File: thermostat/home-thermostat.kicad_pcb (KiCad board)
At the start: 2 copper layers, 146 x 79.5 mm, 100 parts, among them J1 Thermosthat, J2 Conn_01x24, J3 Conn_01x06, J4 AVR-ISP-6, Q1 BC817, Q2 BC817, Q3 BSS806NL6327, Q4 BC817, Q5 BSS806NL6327, Q6 BC817, Q7 BSS806NL6327, SW1 UP, SW2 DOWN, SW3 LEFT, SW4 RIGHT, SW5 OK, SW6 CANCEL, U1 ESP-12F, U2 MCP7940N-xMS, U3 LM2574M-5, U4 LD1117S33TR_SOT223, U5 AT24C512, U6 ATmega328P-AU, U7 LM358, U8 MCP9844, Y1 GEY KX-327NHT 12, Y2 20MHz ABM3B

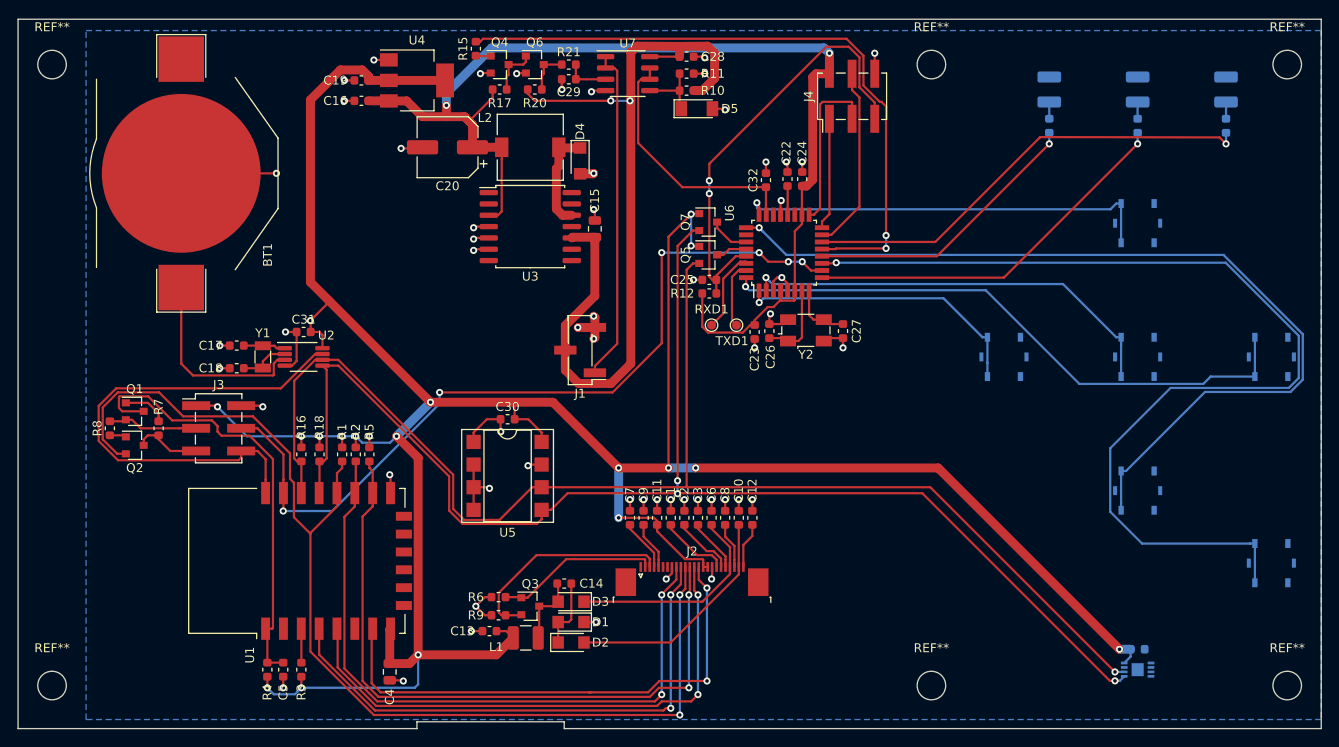
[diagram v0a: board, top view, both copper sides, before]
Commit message: Updated symbols after library update, some footprints still need to be assigned. Deleted PCB except for Display and buttons. Button arrangement wrong. Move buttons to other side of Display. Maybe put buttons on separate PCB and create one PCB for MCU and logic, since that needs to be a four layer one. That is expensive and should be kept as small as possible.
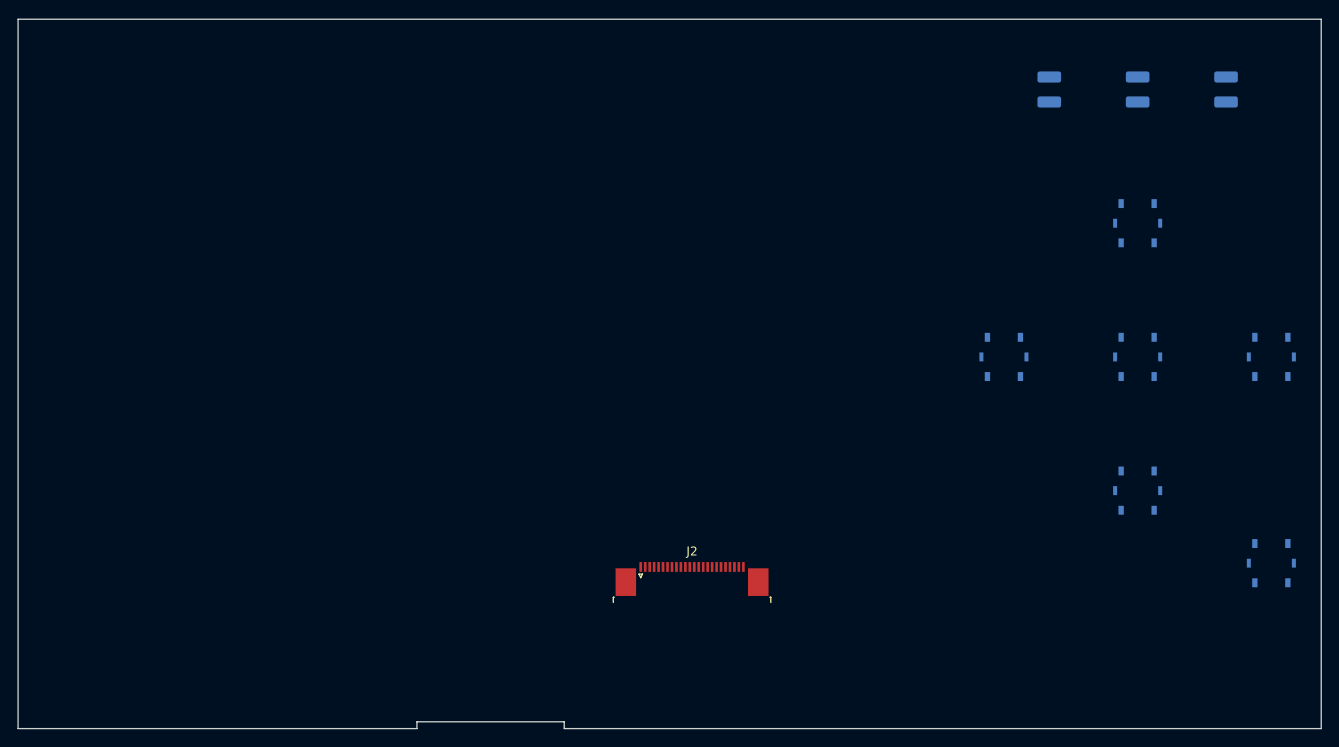
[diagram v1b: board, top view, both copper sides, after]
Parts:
- removed BT1: Battery_Cell, Battery:BatteryHolder_Keystone_3002_1x2032
- removed C1, C10, C12, C2, C29, C3, C6, C7, C8, C9: 1u, Capacitor_SMD:C_0603_1608Metric
- removed C11, C14, C16, C22, C23, C24, C28, C5: 100n, Capacitor_SMD:C_0603_1608Metric
- removed C13: 4u7, Capacitor_SMD:C_0603_1608Metric
- removed C15: 22u, Capacitor_SMD:C_0805_2012Metric
- removed C17, C18: 10p, Capacitor_SMD:C_0603_1608Metric
- removed C19: 2u2, Capacitor_SMD:C_0603_1608Metric
- removed C20: 220u, Capacitor_SMD:CP_Elec_6.3x5.4
- removed C21, C30, C31, C32: 10n, Capacitor_SMD:C_0603_1608Metric
- removed C25: 47n, Capacitor_SMD:C_0603_1608Metric
- removed C26, C27: 15p, Capacitor_SMD:C_0603_1608Metric
- removed C4: 100u, Capacitor_SMD:C_0805_2012Metric
- removed D1, D2, D3, D4: SL03, Diode_SMD:D_SMF
- removed D5: ZMM3V3, Diode_SMD:D_MiniMELF
- removed J1: Thermosthat, Connector_PinHeader_2.54mm:PinHeader_1x03_P2.54mm_Vertical_SMD_Pin1Left
- removed J3: Conn_01x06, Connector_PinHeader_2.54mm:PinHeader_2x03_P2.54mm_Vertical_SMD
- removed J4: AVR-ISP-6, Connector_PinHeader_2.54mm:PinHeader_2x03_P2.54mm_Vertical_SMD
- removed L1: 68u, Inductor_SMD:L_1210_3225Metric
- removed L2: 330u, Inductor_SMD:L_7.3x7.3_H3.5
- removed Q1, Q2, Q4, Q6: BC817, Package_TO_SOT_SMD:SOT-23
- removed Q3, Q5, Q7: BSS806NL6327, Package_TO_SOT_SMD:SOT-23
- removed R1, R10, R12, R2, R20, R3, R4, R5, R6, R7, R8: 10K, Resistor_SMD:R_0603_1608Metric
- removed R11, R21: 1K, Resistor_SMD:R_0603_1608Metric
- removed R13, R14, R19: 1K8, Resistor_SMD:R_0603_1608Metric
- removed R15, R16, R17, R18: 4K7, Resistor_SMD:R_0603_1608Metric
- removed R9: 0.47R, Resistor_SMD:R_0603_1608Metric
- removed REF** (x6): MountingHole_3.2mm_M3, MountingHole:MountingHole_3.2mm_M3
- removed RXD1: RXD, TestPoint:TestPoint_Pad_D1.0mm
- removed TXD1: TXD, TestPoint:TestPoint_Pad_D1.0mm
- removed U1: ESP-12F, RF_Module:ESP-12E
- removed U2: MCP7940N-xMS, Package_SO:MSOP-8_3x3mm_P0.65mm
- removed U3: LM2574M-5, Package_SO:SOIC-14W_7.5x9mm_P1.27mm
- removed U4: LD1117S33TR_SOT223, Package_TO_SOT_SMD:SOT-223-3_TabPin2
- removed U5: AT24C512, Package_DIP:DIP-8_W7.62mm_SMDSocket_SmallPads
- removed U6: ATmega328P-AU, Package_QFP:TQFP-32_7x7mm_P0.8mm
- removed U7: LM358, Package_SO:SOIC-8_3.9x4.9mm_P1.27mm
- removed U8: MCP9844, Package_DFN_QFN:DFN-8-1EP_3x2mm_P0.5mm_EP1.36x1.46mm
- removed Y1: GEY KX-327NHT 12, Crystal:Crystal_SMD_3215-2Pin_3.2x1.5mm
- removed Y2: 20MHz ABM3B, Crystal:Crystal_SMD_Abracon_ABM3B-4Pin_5.0x3.2mm
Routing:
- net +3V3: track 321.8 -> 0.00 mm, vias 18 -> 0
- net /SDA: track 156.5 -> 0.00 mm, vias 3 -> 0
- net /SCL: track 153.1 -> 0.00 mm, vias 1 -> 0
- net +5V: track 127.6 -> 0.00 mm, vias 2 -> 0
- net /GPIO0: track 125.3 -> 0.00 mm, vias 2 -> 0
- net /regulator_out/CANCEL: track 115.2 -> 0.00 mm, vias 1 -> 0
- net GND: track 112.8 -> 0.00 mm, vias 56 -> 0
- net /regulator_out/DOWN: track 101.4 -> 0.00 mm, vias 1 -> 0
- net +36V: track 95.3 -> 0.00 mm, vias 2 -> 0
- net /AVR_INT: track 92.2 -> 0.00 mm, vias 6 -> 0
- net /GPIO15: track 76.6 -> 0.00 mm, vias 2 -> 0
- net /GPIO2: track 76.1 -> 0.00 mm, vias 2 -> 0
- net /regulator_out/pwm_sig: track 74.3 -> 0.00 mm, vias 2 -> 0
- net /regulator_out/LEFT: track 67.4 -> 0.00 mm, vias 1 -> 0
- net /SCK: track 61.5 -> 0.00 mm, vias 2 -> 0
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- removed copper zone on B.Cu, net GND

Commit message: Finalized Thermostat circuit based on the MKW41Z.
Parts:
- added BT1: Battery_Cell, Battery:BatteryHolder_Keystone_3002_1x2032, F.Cu at (49.4, 33.8)
- added C1: 0,1u, Capacitor_SMD:C_0402_1005Metric, F.Cu at (34.5, 77.1)
- added C10: 0,1u, Capacitor_SMD:C_0402_1005Metric, F.Cu at (52.7, 76.9)
- added C11: 0,1u, Capacitor_SMD:C_0402_1005Metric, F.Cu at (55.6, 76.9)
- added C12: 0, Capacitor_SMD:C_0603_1608Metric, F.Cu at (45.4, 46.7)
- added C13: 10p, Capacitor_SMD:C_0402_1005Metric, F.Cu at (76.7, 62.3)
- added C14: 1n, Capacitor_SMD:C_0603_1608Metric, F.Cu at (58.9, 69.2)
- added C15: 1u, Capacitor_SMD:C_0603_1608Metric, F.Cu at (138.1, 35.0)
- added C16: 1u, Capacitor_SMD:C_0603_1608Metric, F.Cu at (142.1, 34.2)
- added C17: 1u, Capacitor_SMD:C_0603_1608Metric, F.Cu at (150.1, 36.9)
- added C18: 1u, Capacitor_SMD:C_0603_1608Metric, F.Cu at (134.1, 35.0)
- added C19: 1u, Capacitor_SMD:C_0603_1608Metric, F.Cu at (150.1, 34.4)
- added C2: 10u, Capacitor_SMD:C_0603_1608Metric, F.Cu at (58.9, 71.8)
- added C20: 1u, Capacitor_SMD:C_0603_1608Metric, F.Cu at (140.0, 31.7)
- added C21: 1u, Capacitor_SMD:C_0603_1608Metric, F.Cu at (146.1, 36.9)
- added C22: 1u, Capacitor_SMD:C_0603_1608Metric, F.Cu at (150.1, 31.9)
- added C23: 100n, Capacitor_SMD:C_0603_1608Metric, F.Cu at (146.1, 34.4)
- added C24: 1u, Capacitor_SMD:C_0603_1608Metric, F.Cu at (152.4, 27.3)
- added C25: 10u, Capacitor_SMD:C_0603_1608Metric, F.Cu at (146.1, 31.9)
- added C26: 4u7, Capacitor_SMD:C_0603_1608Metric, F.Cu at (134.1, 37.5)
- added C27: 10n, Capacitor_SMD:C_0603_1608Metric, F.Cu at (75.2, 35.8)
- added C28: 0, Capacitor_SMD:C_0603_1608Metric, F.Cu at (61.4, 46.7)
- added C29: 0,1u, Capacitor_SMD:C_0603_1608Metric, F.Cu at (46.3, 77.1)
- added C3: 1u, Capacitor_SMD:C_0402_1005Metric, F.Cu at (58.5, 76.5)
- added C30: 10n, Capacitor_SMD:C_0603_1608Metric, F.Cu at (49.4, 46.7)
- added C31: 1u, Capacitor_SMD:C_0603_1608Metric, F.Cu at (53.4, 46.7)
- added C32: 22u, Capacitor_SMD:C_0805_2012Metric, F.Cu at (117.1, 56.9)
- added C33: 100n, Capacitor_SMD:C_0603_1608Metric, F.Cu at (116.2, 62.2)
- added C34: 2u2, Capacitor_SMD:C_0603_1608Metric, F.Cu at (116.9, 59.6)
- added C35: 220u, Capacitor_SMD:CP_Elec_6.3x5.4, F.Cu at (88.0, 66.7)
- added C36: 10n, Capacitor_SMD:C_0603_1608Metric, F.Cu at (107.8, 71.2)
- added C37: 1u, Capacitor_SMD:C_0603_1608Metric, F.Cu at (103.3, 73.2)
- added C38: 100n, Capacitor_SMD:C_0603_1608Metric, F.Cu at (107.8, 68.6)
- added C39: 1n, Capacitor_SMD:C_0603_1608Metric, F.Cu at (88.9, 43.3)
- added C4: 0,1u, Capacitor_SMD:C_0402_1005Metric, F.Cu at (65.4, 74.6)
- added C40: 1n, Capacitor_SMD:C_0603_1608Metric, F.Cu at (110.1, 40.0)
- added C41: 1n, Capacitor_SMD:C_0603_1608Metric, F.Cu at (110.1, 42.5)
- added C42: 1n, Capacitor_SMD:C_0603_1608Metric, F.Cu at (117.7, 33.9)
- added C43: 1n, Capacitor_SMD:C_0603_1608Metric, F.Cu at (114.1, 38.5)
- added C44: 1n, Capacitor_SMD:C_0603_1608Metric, F.Cu at (114.1, 41.0)
- added C45: 100n, Capacitor_SMD:C_0603_1608Metric, F.Cu at (118.2, 36.4)
- added C46: 1u, Capacitor_SMD:C_0603_1608Metric, F.Cu at (75.6, 53.3)
- added C47: 1u, Capacitor_SMD:C_0603_1608Metric, F.Cu at (75.2, 57.0)
- added C48: 0,1u, Capacitor_SMD:C_0603_1608Metric, F.Cu at (62.9, 68.7)
- added C49: 1u, Capacitor_SMD:C_0603_1608Metric, F.Cu at (111.8, 66.7)
- added C5: 10p, Capacitor_SMD:C_0402_1005Metric, F.Cu at (69.4, 68.2)
- added C6: 12p, Capacitor_SMD:C_0402_1005Metric, F.Cu at (69.2, 66.2)
- added C7: 12p, Capacitor_SMD:C_0402_1005Metric, F.Cu at (69.4, 70.2)
- added C8: 1u, Capacitor_SMD:C_0603_1608Metric, F.Cu at (70.2, 60.3)
- added C9: 0,7p, Capacitor_SMD:C_0402_1005Metric, F.Cu at (49.8, 76.9)
- added D1: LED, LED_SMD:LED_1210_3225Metric, F.Cu at (41.5, 74.4)
- added D2: SL03, Diode_SMD:D_SMF, F.Cu at (135.1, 32.1)
- added D3: SL03, Diode_SMD:D_SMF, F.Cu at (148.9, 24.4)
- added D4: SL03, Diode_SMD:D_SMF, F.Cu at (129.4, 32.1)
- added D5: SL03, Diode_SMD:D_SMF, F.Cu at (117.8, 53.8)
- added D9: RED, LED_SMD:LED_1210_3225Metric, F.Cu at (100.9, 39.8)
- added J1: Amphenol_132289 SMA, Connector_Coaxial:SMA_Amphenol_132289_EdgeMount, F.Cu at (37.3, 58.2)
- added J3: Thermosthat, Connector_PinHeader_2.54mm:PinHeader_1x03_P2.54mm_Vertical_SMD_Pin1Left, F.Cu at (97.3, 67.5)
- added JP1: SolderJumper_3_Open, Jumper:SolderJumper-3_P1.3mm_Open_Pad1.0x1.5mm, F.Cu at (35.9, 74.0)
- added JP2: SolderJumper_2_Open, Jumper:SolderJumper-2_P1.3mm_Open_Pad1.0x1.5mm, F.Cu at (46.5, 74.0)
- added L1: 0,1u, Inductor_SMD:L_0402_1005Metric, F.Cu at (61.4, 77.1)
- added L2: 5,6n, Inductor_SMD:L_0402_1005Metric, F.Cu at (72.2, 66.2)
- added L3: 68u, Inductor_SMD:L_1210_3225Metric, F.Cu at (129.3, 35.9)
- added L4: 330u, Inductor_SMD:L_7.3x7.3_H3.5, F.Cu at (110.2, 56.5)
- added L5: 0,1u, Inductor_SMD:L_0402_1005Metric, F.Cu at (72.3, 68.2)
- added Q1: BSS806NL6327, Package_TO_SOT_SMD:SOT-23, F.Cu at (148.2, 28.3)
- added Q2: BC817, Package_TO_SOT_SMD:SOT-23, F.Cu at (112.0, 63.2)
- added Q3: BC817, Package_TO_SOT_SMD:SOT-23, F.Cu at (103.5, 69.7)
- added Q4: BC817, Package_TO_SOT_SMD:SOT-23, F.Cu at (105.9, 41.0)
- added Q5: BC817, Package_TO_SOT_SMD:SOT-23, F.Cu at (120.7, 25.0)
- added Q6: BC817, Package_TO_SOT_SMD:SOT-23, F.Cu at (113.5, 32.4)
- added R10: 4K7, Resistor_SMD:R_0603_1608Metric, F.Cu at (116.2, 64.7)
- added R11: 10K, Resistor_SMD:R_0603_1608Metric, F.Cu at (111.8, 69.3)
- added R12: 1K, Resistor_SMD:R_0603_1608Metric, F.Cu at (91.1, 72.0)
- added R13: 0, Resistor_SMD:R_0603_1608Metric, F.Cu at (93.0, 43.3)
- added R14: 0, Resistor_SMD:R_0603_1608Metric, F.Cu at (97.0, 43.3)
- added R15: 0, Resistor_SMD:R_0603_1608Metric, F.Cu at (101.0, 43.2)
- added R16: 100k, Resistor_SMD:R_0603_1608Metric, F.Cu at (120.5, 28.5)
- added R17: 100k, Resistor_SMD:R_0603_1608Metric, F.Cu at (113.2, 36.0)
- added R18: 100k, Resistor_SMD:R_0603_1608Metric, F.Cu at (117.7, 31.4)
- added R19: 100k, Resistor_SMD:R_0603_1608Metric, F.Cu at (84.9, 43.3)
- added R2: 0, Resistor_SMD:R_0603_1608Metric, F.Cu at (58.9, 74.3)
- added R3: 10K, Resistor_SMD:R_0603_1608Metric, F.Cu at (142.1, 36.7)
- added R4: 0.47R, Resistor_SMD:R_0603_1608Metric, F.Cu at (138.1, 37.5)
- added R5: 2k2, Resistor_SMD:R_0603_1608Metric, F.Cu at (67.8, 40.4)
- added R6: 2k2, Resistor_SMD:R_0603_1608Metric, F.Cu at (57.4, 46.7)
- added R7: 10K, Resistor_SMD:R_0603_1608Metric, F.Cu at (120.2, 64.7)
- added R8: 1K, Resistor_SMD:R_0603_1608Metric, F.Cu at (115.8, 67.2)
- added R9: 4K7, Resistor_SMD:R_0603_1608Metric, F.Cu at (120.2, 62.2)
- added SW7: CANCEL, Button_Switch_SMD:SW_SPST_Panasonic_EVQPL_3PL_5PL_PT_A08, F.Cu at (114.7, 26.4)
- added TP1: TestPoint, TestPoint:TestPoint_Pad_D1.0mm, F.Cu at (50.5, 65.8)
- added TP10: ~RST, TestPoint:TestPoint_Pad_D1.0mm, F.Cu at (62.4, 74.6)
- added TP11: SWD_DIO, TestPoint:TestPoint_Pad_D1.0mm, F.Cu at (66.4, 69.0)
- added TP12: SWD_CLK, TestPoint:TestPoint_Pad_D1.0mm, F.Cu at (76.8, 59.8)
- added TP13: UART_TX, TestPoint:TestPoint_Pad_D1.0mm, F.Cu at (73.7, 60.6)
- added TP14: SUPPLY_V, TestPoint:TestPoint_Pad_D1.0mm, F.Cu at (62.4, 71.5)
- added TP2: TestPoint, MountingHole:MountingHole_3.2mm_M3, F.Cu at (64.2, 56.1)
- added TP3: TestPoint, MountingHole:MountingHole_3.2mm_M3, F.Cu at (37.0, 68.3)
- added TP4: TestPoint, MountingHole:MountingHole_3.2mm_M3, F.Cu at (45.0, 68.3)
- added TP5: TestPoint, MountingHole:MountingHole_3.2mm_M3, F.Cu at (56.3, 56.1)
- added TP6: TestPoint, MountingHole:MountingHole_3.2mm_M3, F.Cu at (56.3, 64.0)
- added TP7: TestPoint, MountingHole:MountingHole_3.2mm_M3, F.Cu at (52.9, 72.0)
- added TP8: 3V3, TestPoint:TestPoint_Pad_D1.0mm, F.Cu at (65.5, 72.1)
- added TP9: GND, TestPoint:TestPoint_Pad_D1.0mm, F.Cu at (73.2, 63.7)
- added U1: MKW41Z512VHT, Package_DFN_QFN:NXP_LQFN-48-1EP_7x7mm_P0.5mm_EP3.5x3.5mm_16xMask0.45x0.45_ThermalVias, F.Cu at (71.1, 106.0)
- added U2: MCP7940N-xMS, Package_SO:MSOP-8_3x3mm_P0.65mm, F.Cu at (69.5, 36.8)
- added U3: MCP9844, Package_DFN_QFN:DFN-8-1EP_3x2mm_P0.5mm_EP1.36x1.46mm, F.Cu at (35.7, 47.2)
- added U4: AT24C512, Package_DIP:DIP-8_W7.62mm_SMDSocket_SmallPads, F.Cu at (71.7, 28.6)
- added U5: LM2574M-5, Package_SO:SOIC-14W_7.5x9mm_P1.27mm, F.Cu at (89.2, 57.4)
- added U6: LD1117S33TR_SOT223, Package_TO_SOT_SMD:SOT-223-3_TabPin2, F.Cu at (100.5, 56.2)
- added U7: LM358, Package_SO:SOIC-8_3.9x4.9mm_P1.27mm, F.Cu at (105.5, 64.2)
- added U8: PCF8574, Package_SO:SOIC-16W_7.5x10.3mm_P1.27mm, F.Cu at (89.4, 28.6)
- added U9: SN74LVC2T45DCUR, Package_SO:VSSOP-8_2.4x2.1mm_P0.5mm, F.Cu at (70.9, 53.9)
- added Y1: 32MHz 10PPM SMT 2.0x1.6mm 10PF, Crystal:Crystal_SMD_2016-4Pin_2.0x1.6mm, F.Cu at (69.7, 63.4)
- added Y2: 32.768KHz 20PPM 3.2x1.5mm 7PF, Crystal:Crystal_SMD_3215-2Pin_3.2x1.5mm, F.Cu at (70.7, 57.4)
- added Y3: 32.768KHz 20PPM 3.2x1.5mm 7PF, Crystal:Crystal_SMD_3215-2Pin_3.2x1.5mm, F.Cu at (40.9, 47.1)
- D6: value YELLOW -> ZMM3V3; footprint LED_SMD:LED_1210_3225Metric -> Diode_SMD:D_MiniMELF; moved to F.Cu
- D7: value RED -> YELLOW; moved to F.Cu
- D8: moved to F.Cu
- SW1: value UP -> SW_Push; moved to F.Cu
- SW2: value DOWN -> UP; moved to F.Cu
- SW3: value LEFT -> DOWN; moved to F.Cu
- SW4: value RIGHT -> LEFT; moved to F.Cu
- SW5: value OK -> RIGHT; moved to F.Cu
- SW6: value CANCEL -> OK; moved to F.Cu
- moved J2 242.0 mm to (-68.7, 26.9)
- moved Waveshare 4.2 Inch raw panel 241.7 mm to (-91.2, 4.70)
- moved SW6 156.9 mm to (101.8, 33.9)
- moved SW2 147.4 mm to (86.7, 38.3)
- moved SW3 146.4 mm to (99.6, 26.4)
- moved SW1 132.2 mm to (64.0, 63.8)
- moved SW5 132.2 mm to (107.2, 26.4)
- moved SW4 121.4 mm to (94.3, 38.3)
- moved D8 111.6 mm to (108.4, 32.3), turned to 0 degrees
- moved D6 103.2 mm to (85.9, 72.4), turned to 0 degrees
- moved D7 94.1 mm to (108.4, 36.6), turned to 0 degrees
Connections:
- net /HLT_CTL renamed /display/HLT_CTL
- net /TSCL renamed /display/TSCL
- net /TSDA renamed /display/TSDA
- D6 pad 1: GND -> Net-(D6-Pad1)
- D6 pad 2: Net-(D6-Pad2) -> GND
- D7 pad 1: GND -> Net-(D7-Pad1)
- D8 pad 1: GND -> Net-(D8-Pad1)
- J2 pad 10: /eink-RST -> /~DP_RST
- J2 pad 11: /GPIO0 -> GND
- J2 pad 12: /GPIO15 -> /SPI1_PCS0
- J2 pad 13: /SCK -> /SPI1_SCK
- J2 pad 14: /MOSI -> /SPI1_MOSI
- J2 pad 18: /VDD -> /display/VDD
- J2 pad 19: /VPP -> /display/VPP
- J2 pad 2: /GDR -> /display/GDR
- J2 pad 20: /VSH -> /display/VSH
- J2 pad 21: /PREVGH -> /display/PREVGH
- J2 pad 22: /VSL -> /display/VSL
- J2 pad 23: /PREVGL -> /display/PREVGL
- J2 pad 24: /VCOM -> /display/VCOM
- J2 pad 3: /RESE -> /display/RESE
- J2 pad 4: /VGL -> /display/VGL
- J2 pad 5: /VGH -> /display/VGH
- J2 pad 8: GND -> +3V3
- J2 pad 9: /GPIO2 -> /DP_BUSY
- SW1 pad 1: /regulator_out/UP -> GND
- SW1 pad 2: GND -> /RESET_b
- SW2 pad 1: /regulator_out/DOWN -> /GPIO/BTN_UP
- SW3 pad 1: /regulator_out/LEFT -> /GPIO/BTN_DOWN
- SW4 pad 1: /regulator_out/RIGHT -> /GPIO/BTN_LEFT
- SW5 pad 1: /regulator_out/OK -> /GPIO/BTN_RIGHT
- SW6 pad 1: /regulator_out/CANCEL -> /BTN_OK

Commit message: Started grouping footprints on PCB, configured minimal via and trace sizes for PCB_POOL.
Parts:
- added C50: 0,1u, Capacitor_SMD:C_0402_1005Metric, F.Cu at (231.8, 106.8)
- added C51: 10u, Capacitor_SMD:C_0603_1608Metric, F.Cu at (232.8, 109.1)
- added C52: 1u, Capacitor_SMD:C_0402_1005Metric, F.Cu at (225.2, 107.4)
- added C53: 1u, Capacitor_SMD:C_0402_1005Metric, F.Cu at (225.7, 96.0)
- added C54: 10u, Capacitor_SMD:C_0603_1608Metric, F.Cu at (225.2, 109.7)
- added C55: 10u, Capacitor_SMD:C_0603_1608Metric, F.Cu at (225.7, 93.7)
- added L6: 0,1u, Inductor_SMD:L_0402_1005Metric, F.Cu at (224.2, 107.4)
- added L7: 0,1u, Inductor_SMD:L_0402_1005Metric, F.Cu at (226.7, 96.0)
- added TP15: 5V, TestPoint:TestPoint_Pad_D1.0mm, F.Cu at (58.9, 78.2)
- C8: footprint Capacitor_SMD:C_0603_1608Metric -> Capacitor_SMD:C_0402_1005Metric
- moved U3 241.5 mm to (256.8, 144.4)
- moved C30 227.7 mm to (256.8, 140.7)
- moved J1 214.9 mm to (248.0, 100.2)
- moved C1 185.2 mm to (218.6, 97.7)
- moved C9 182.6 mm to (231.0, 99.7), turned to 90 degrees
- moved C10 176.1 mm to (226.2, 107.4), turned to 270 degrees
- moved L1 174.9 mm to (233.8, 106.8), turned to 270 degrees
- moved C3 174.8 mm to (232.0, 97.5), turned to 90 degrees
- moved C2 174.7 mm to (232.0, 95.2)
- moved BT1 172.8 mm to (127.1, 188.1)
- moved C13 170.4 mm to (242.8, 100.2), turned to 180 degrees
- moved C4 170.2 mm to (233.4, 101.5)
- moved C31 170.2 mm to (198.4, 135.8)
- moved C11 170.1 mm to (224.7, 96.0), turned to 90 degrees
- moved C8 169.1 mm to (232.8, 106.8), turned to 270 degrees
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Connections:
- net Net-(C1-Pad1) renamed /VREF
- net Net-(C3-Pad1) renamed /VDD_RF
- net Net-(C5-Pad1) renamed /XTAL_O
- net Net-(C8-Pad1) renamed /VDDA
- C10 pad 1: +3V3 -> /VDD_0
- C11 pad 1: +3V3 -> /VDD_1
- U1 pad 20: +3V3 -> /VDD_0
- U1 pad 44: +3V3 -> /VDD_1
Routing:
- net /VDDA: track 0.00 -> 5.29 mm
- net Net-(U1-Pad30): track 0.00 -> 5.25 mm
- net /XTAL_O: track 0.00 -> 4.49 mm, vias 0 -> 1
- net /VDD_0: track 0.00 -> 4.17 mm
- net Net-(U1-Pad31): track 0.00 -> 3.09 mm
- net /VDD_RF: track 0.00 -> 2.03 mm
- net /VREF: track 0.00 -> 0.92 mm, vias 0 -> 1
- net (no net): vias 0 -> 16
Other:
- copper layers 2 -> 4
- net class Default: clearance 0.2 -> 0.15; trace_width 0.25 -> 0.15; via_dia 0.8 -> 0.5; via_drill 0.4 -> 0.2
- rule trace_clearance: 0.2 -> 0.15
- rule trace_min: 0.2 -> 0.15
- rule via_min_drill: 0.3 -> 0.2
- rule via_min_size: 0.4 -> 0.5

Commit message: Started routing some subgroups, going to put GPIO on other board and not attach display directly, as that would make the PCB too large and expensive.
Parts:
- removed Waveshare 4.2 Inch raw panel: waveshare_4.2_raw_panel, myfootprints:waveshare_4.2_raw_panel_folded_connector
- moved C14 314.3 mm to (286.8, -86.1)
- moved C29 314.3 mm to (310.5, -36.7)
- moved C30 314.3 mm to (512.8, -41.7)
- moved C31 314.3 mm to (454.4, -46.6)
- moved C32 314.3 mm to (496.6, -137.0)
- moved C33 314.3 mm to (473.0, -143.1)
- moved C34 314.3 mm to (467.7, -143.8)
- moved C35 314.3 mm to (494.9, -152.1)
- moved C37 314.3 mm to (444.1, -123.4)
- moved C38 314.3 mm to (456.6, -126.0)
- moved C39 314.3 mm to (345.0, -139.1)
- moved C40 314.3 mm to (366.2, -142.4)
- moved C41 314.3 mm to (366.2, -139.9)
- moved C42 314.3 mm to (373.7, -148.4)
- moved C43 314.3 mm to (370.2, -143.9)
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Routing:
- net +3V3: track 0.00 -> 14.7 mm
- net Net-(C26-Pad1): track 0.00 -> 12.2 mm
- net Net-(C26-Pad2): track 0.00 -> 7.80 mm
- net /display/VDD: track 0.00 -> 7.06 mm
- net /display/GDR: track 0.00 -> 6.91 mm
- net /display/VCOM: track 0.00 -> 6.86 mm
- net /display/VPP: track 0.00 -> 6.64 mm
- net /display/RESE: track 0.00 -> 6.48 mm
- net /display/PREVGL: track 0.00 -> 6.28 mm
- net /display/VSH: track 0.00 -> 6.22 mm
- net /display/VGL: track 0.00 -> 6.06 mm
- net /display/VSL: track 0.00 -> 5.85 mm
- net /display/PREVGH: track 0.00 -> 5.79 mm
- net /display/VGH: track 0.00 -> 5.63 mm
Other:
- board outline removed

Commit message: Fine grouping of parts done, may start routing . GPIO connector on wrong side of PCB (I wanted to have the buttons on the opposite side, but thats not a big problem.
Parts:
- removed D8: GREEN, LED_SMD:LED_1210_3225Metric
- removed D9: RED, LED_SMD:LED_1210_3225Metric
- removed SW1: SW_Push, Button_Switch_SMD:SW_SPST_Panasonic_EVQPL_3PL_5PL_PT_A08
- removed SW2: UP, Button_Switch_SMD:SW_SPST_Panasonic_EVQPL_3PL_5PL_PT_A08
- removed SW3: DOWN, Button_Switch_SMD:SW_SPST_Panasonic_EVQPL_3PL_5PL_PT_A08
- removed SW4: LEFT, Button_Switch_SMD:SW_SPST_Panasonic_EVQPL_3PL_5PL_PT_A08
- removed SW5: RIGHT, Button_Switch_SMD:SW_SPST_Panasonic_EVQPL_3PL_5PL_PT_A08
- removed SW6: OK, Button_Switch_SMD:SW_SPST_Panasonic_EVQPL_3PL_5PL_PT_A08
- removed SW7: CANCEL, Button_Switch_SMD:SW_SPST_Panasonic_EVQPL_3PL_5PL_PT_A08
- removed TP10: ~RST, TestPoint:TestPoint_Pad_D1.0mm
- removed TP11: SWD_DIO, TestPoint:TestPoint_Pad_D1.0mm
- removed TP12: SWD_CLK, TestPoint:TestPoint_Pad_D1.0mm
- removed TP13: UART_TX, TestPoint:TestPoint_Pad_D1.0mm
- removed TP6, TP7: TestPoint, MountingHole:MountingHole_3.2mm_M3
- added C56: 0,1u, Capacitor_SMD:C_0402_1005Metric, F.Cu at (155.7, 80.9)
- added C57: 1u, Capacitor_SMD:C_0402_1005Metric, F.Cu at (155.7, 79.9)
- added C58: 1u, Capacitor_SMD:C_0402_1005Metric, F.Cu at (158.0, 79.9)
- added C59: 0,1u, Capacitor_SMD:C_0402_1005Metric, F.Cu at (158.0, 80.9)
- added J4: Conn_ARM_JTAG_SWD_10, Connector_PinHeader_1.27mm:PinHeader_2x05_P1.27mm_Vertical_SMD, F.Cu at (142.6, 100.8)
- added J5: Conn_01x20, Connector_PinHeader_2.54mm:PinHeader_2x10_P2.54mm_Vertical_SMD, F.Cu at (133.7, 85.1)
- added J6: Conn_02x02_Odd_Even, Connector_PinHeader_2.54mm:PinHeader_2x02_P2.54mm_Vertical_SMD, F.Cu at (97.0, 119.6)
- added J7: Thermosthat, Connector_PinHeader_2.54mm:PinHeader_1x03_P2.54mm_Vertical_SMD_Pin1Left, F.Cu at (168.3, 79.8)
- added R1: 0, Resistor_SMD:R_0603_1608Metric, F.Cu at (87.4, 118.0)
- added R20: 0, Resistor_SMD:R_0603_1608Metric, F.Cu at (87.4, 121.3)
- added R21: 100k, Resistor_SMD:R_0402_1005Metric, F.Cu at (126.1, 78.1)
- added R22: 100k, Resistor_SMD:R_0402_1005Metric, F.Cu at (123.6, 78.1)
- added R23: 0?, Resistor_SMD:R_0402_1005Metric, F.Cu at (138.0, 92.8)
- added R24: 0?, Resistor_SMD:R_0402_1005Metric, F.Cu at (133.5, 92.8)
- added R25: 0?, Resistor_SMD:R_0402_1005Metric, F.Cu at (142.6, 92.8)
- added U10: SN74LVC2T45DCUR, Package_SO:VSSOP-8_2.4x2.1mm_P0.5mm, F.Cu at (156.8, 82.8)
- C14, C29, C36, C39, C40, C41, C42, C43, C44, C46, C47, C48: footprint Capacitor_SMD:C_0603_1608Metric -> Capacitor_SMD:C_0402_1005Metric
- C33: value 100n -> 10u
- C34: value 2u2 -> 10u
- D7: value YELLOW -> LED
- R10: value 4K7 -> 4K7?
- R16, R17, R18, R19, R2, R5, R6: footprint Resistor_SMD:R_0603_1608Metric -> Resistor_SMD:R_0402_1005Metric
- R9: value 4K7 -> 0
- U1: footprint Package_DFN_QFN:NXP_LQFN-48-1EP_7x7mm_P0.5mm_EP3.5x3.5mm_16xMask0.45x0.45_ThermalVias -> Package_DFN_QFN:NXP_LQFN-48-1EP_7x7mm_P0.5mm_EP3.5x3.5mm_16xMask0.45x0.45
- moved L4 472.0 mm to (96.5, 78.4), turned to 180 degrees
- moved U5 469.7 mm to (96.5, 87.1)
- moved C35 468.2 mm to (87.4, 78.4), turned to 180 degrees
- moved D5 453.3 mm to (102.0, 79.9), turned to 270 degrees
- moved C32 452.7 mm to (103.5, 87.5), turned to 90 degrees
- moved U6 451.2 mm to (86.1, 88.3), turned to 180 degrees
- moved C34 446.8 mm to (83.2, 83.8)
- moved C33 446.1 mm to (89.0, 83.8), turned to 180 degrees
- moved C49 393.3 mm to (137.9, 106.7), turned to 180 degrees
- moved C38 392.1 mm to (141.0, 106.7), turned to 0 degrees
- moved U7 391.5 mm to (136.1, 110.2)
- moved C37 389.7 mm to (137.8, 117.5)
- moved D6 388.6 mm to (141.1, 110.2), turned to 90 degrees
- moved D7 387.1 mm to (84.2, 121.3)
- moved R12 386.3 mm to (139.3, 117.5), turned to 90 degrees
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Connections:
- C44 pad 1: /BTN_CANCEL -> /GPIO/BTN_CANCEL
- D1 pad 1: /RESET_b -> GND
- D7 pad 1: Net-(D7-Pad1) -> GND
- Q4 pad 1: /TPM0_CH1 -> Net-(Q4-Pad1)
- Q4 pad 3: Net-(D7-Pad1) -> Net-(Q4-Pad3)
- Q5 pad 1: /TPM0_CH3 -> Net-(Q5-Pad1)
- Q5 pad 3: Net-(D8-Pad1) -> Net-(Q5-Pad3)
- Q6 pad 1: /TPM0_CH2 -> Net-(Q6-Pad1)
- Q6 pad 3: Net-(D9-Pad1) -> Net-(Q6-Pad3)
- R13 pad 1: Net-(D7-Pad2) -> Net-(Q4-Pad3)
- R13 pad 2: +3V3 -> /GPIO/YELLOW
- R14 pad 1: Net-(D8-Pad2) -> Net-(Q5-Pad3)
- R14 pad 2: +3V3 -> /GPIO/GREEN
- R15 pad 1: Net-(D9-Pad2) -> Net-(Q6-Pad3)
- R15 pad 2: +3V3 -> /GPIO/RED
- R2 pad 1: Net-(D1-Pad2) -> /RESET_b
- U1 pad 41: Net-(U1-Pad41) -> /BTN_OK
- U1 pad 42: Net-(U1-Pad42) -> /LPUART0_RX
- U8 pad 9: Net-(U8-Pad9) -> /GPIO/BTN_CANCEL
- U9 pad 7: Net-(TP13-Pad1) -> /UART_TX
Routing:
- net /XTAL_O: track 4.49 -> 0.00 mm, vias 1 -> 0
- net /VREF: track 0.92 -> 0.00 mm, vias 1 -> 0
- net /VDDA: track 5.29 -> 4.40 mm
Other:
- board outline added: 142.5 x 50.2 mm
